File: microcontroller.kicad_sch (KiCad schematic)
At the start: 85 parts, among them CN10 JST BM06B-SRSS-TB(LF)(SN), CN11 BM05B-SRSS-TB(LF)(SN), CN2 Samtec FTSH-107-01-L-DV-K, CN3 104031-0811, CN4 M20-9990346, CN5 Molex 105057-0001, CN6 BM03B-SRSS-TB(LF)(SN), CN7 BM04B-SRSS-TB(LF)(SN), CN8 BM04B-SRSS-TB(LF)(SN), CN9 JST BM06B-SRSS-TB(LF)(SN), U2 STM32H743VIT6, U3 TMP102AIDRL, U4 Microchip 24AA256UIDT-I/ST

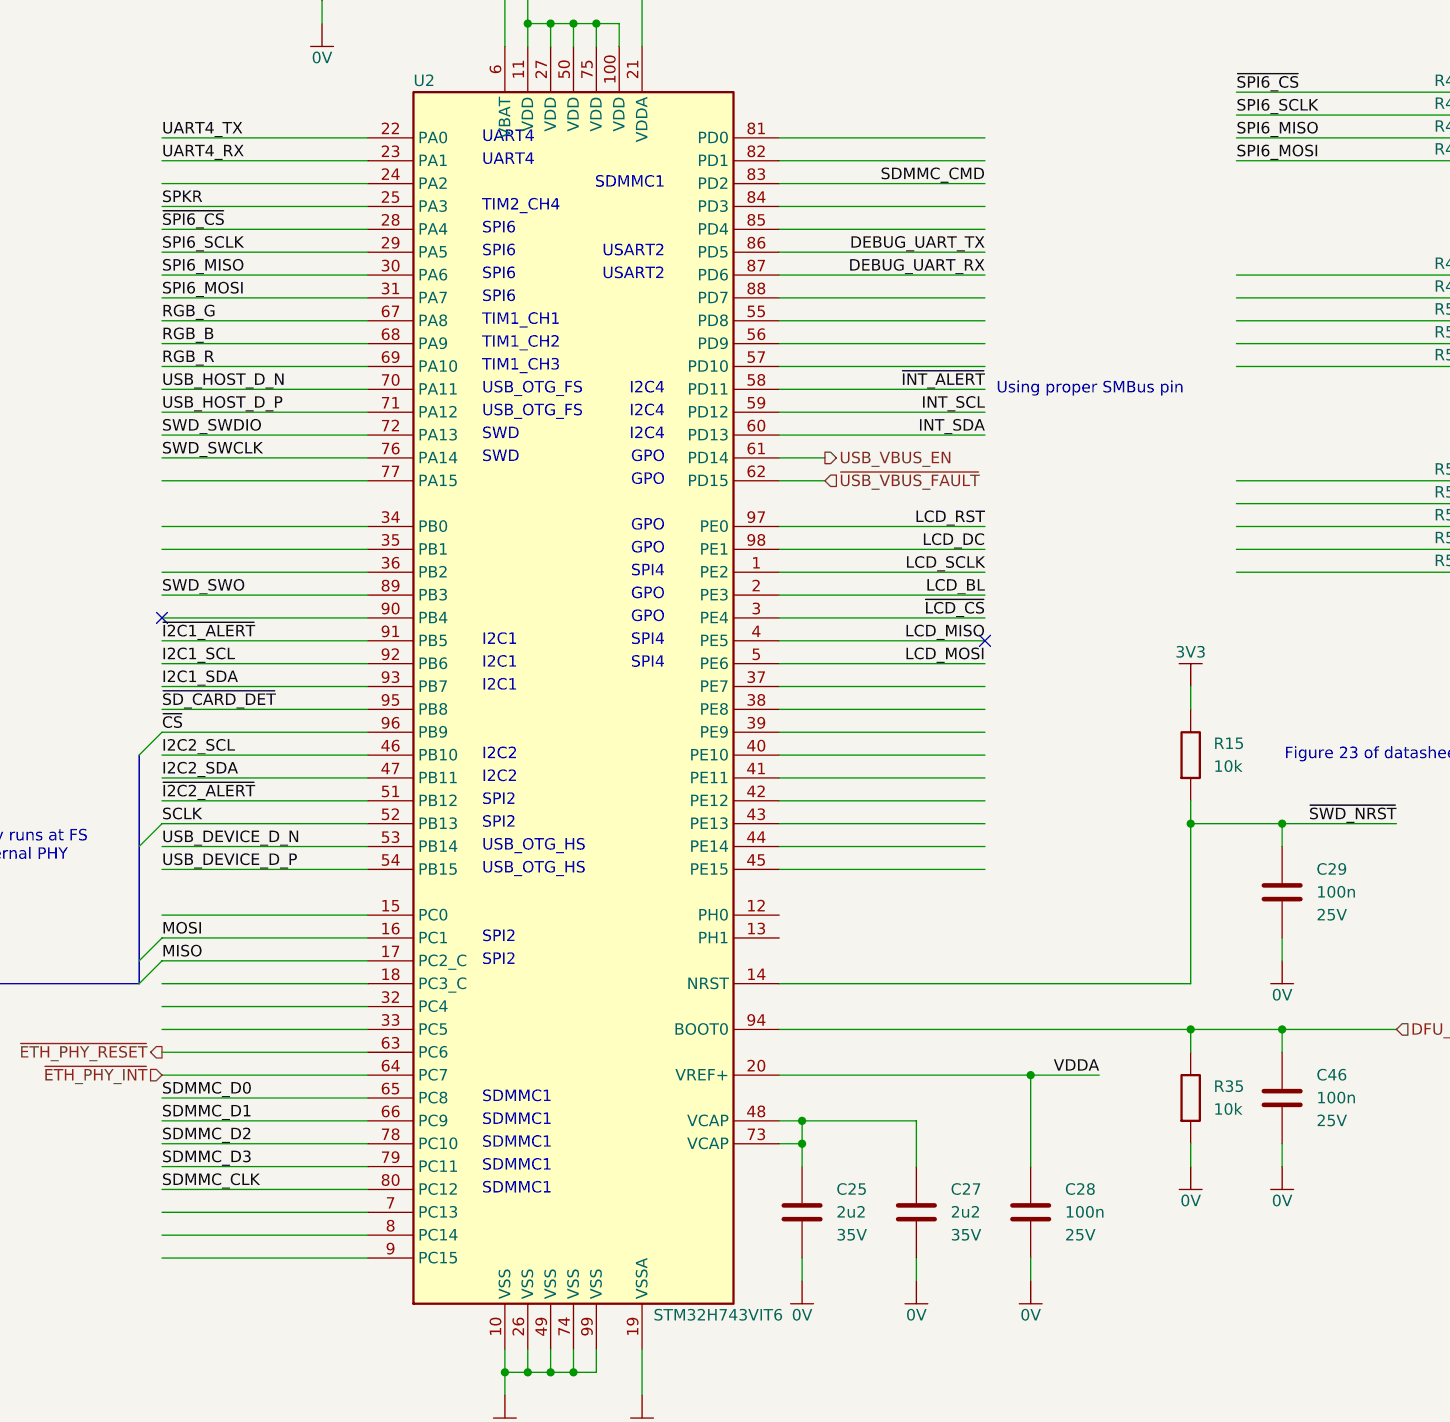
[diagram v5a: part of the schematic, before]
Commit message: headers now connected
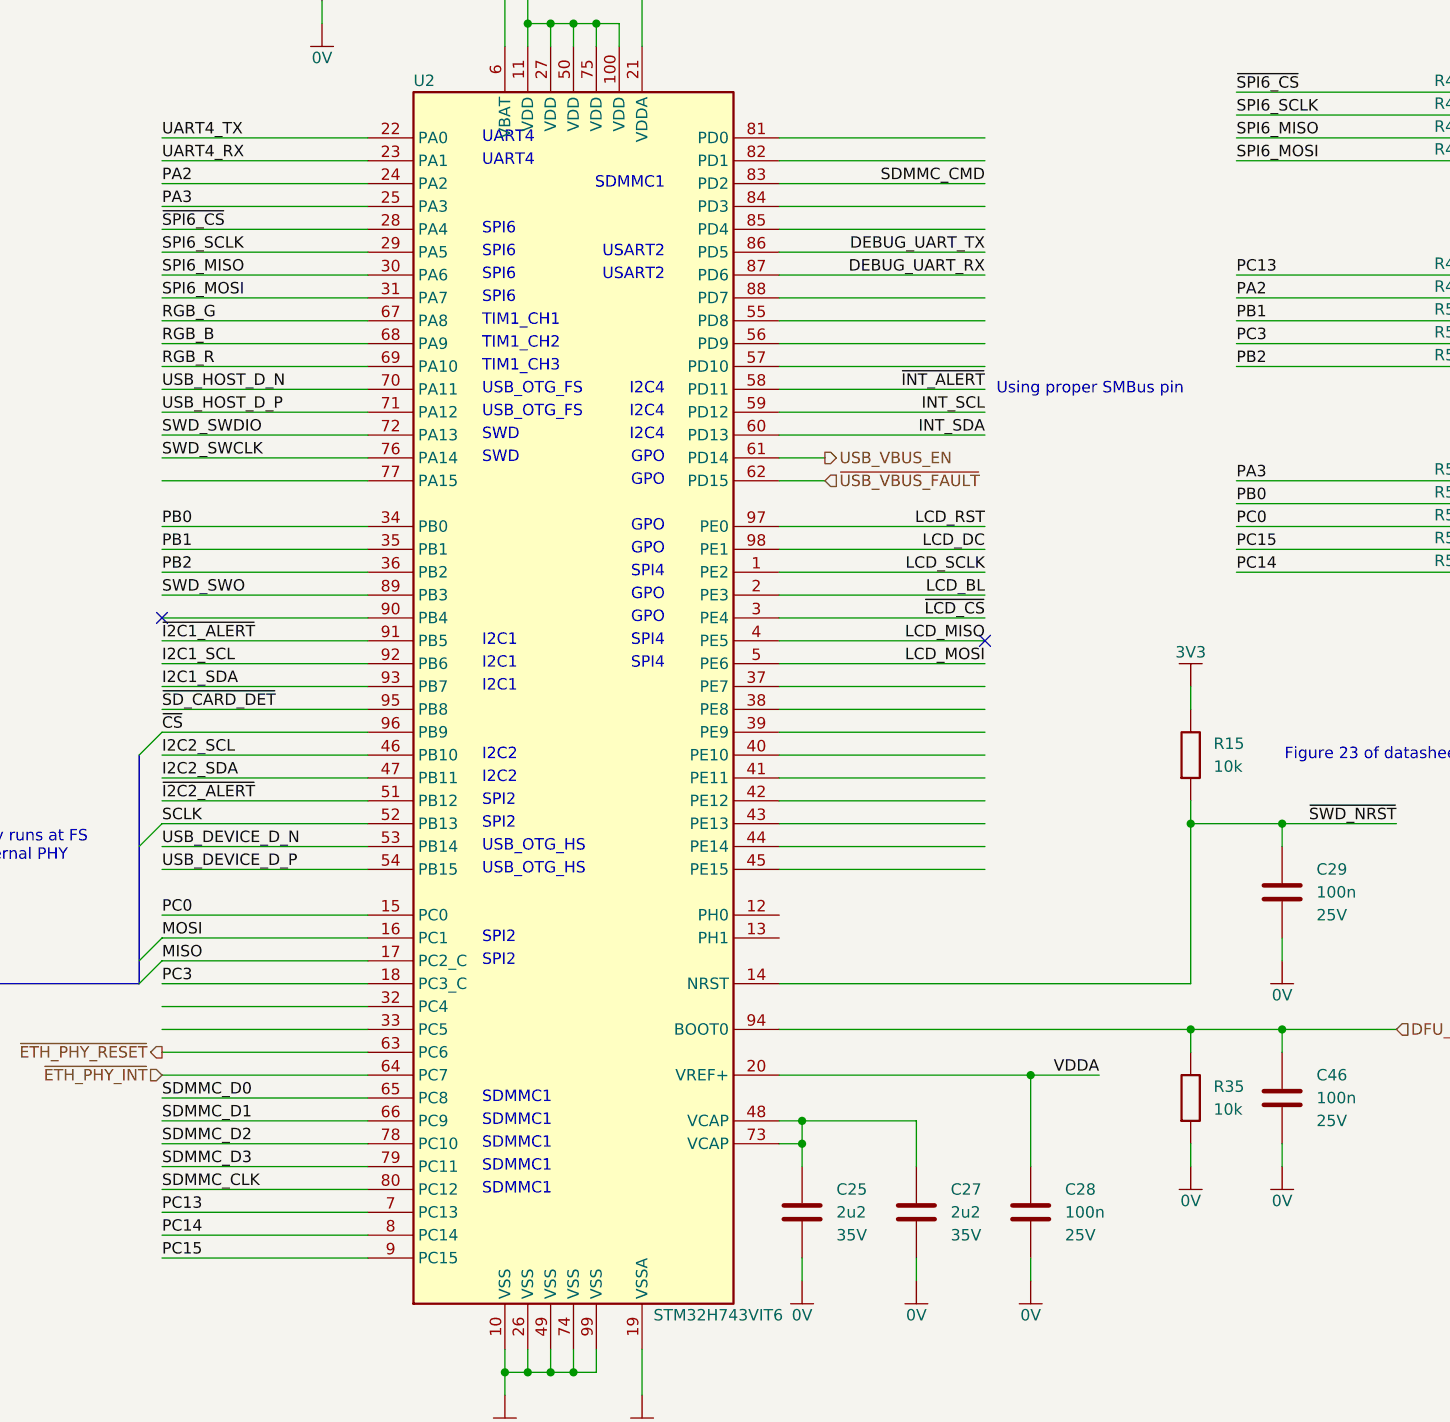
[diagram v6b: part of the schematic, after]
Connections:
- net SPKR is gone; now on net PA3: U2.25 (PA3)
- net PC15: now reaches R56.1
- net PC15: now also U2.9 (PC15)
- net PC14: now reaches R57.1
- net PC14: now also U2.8 (PC14)
- net PC0: now reaches R55.1
- net PC0: now also U2.15 (PC0)
- net PA3: now reaches R53.1
- net PC13: now reaches R48.1
- net PC13: now also U2.7 (PC13)
- net PC3: now reaches R51.1
- net PC3: now also U2.18 (PC3_C)
- net PB0: now reaches R54.1
- net PB0: now also U2.34 (PB0)
- net PB1: now reaches R50.1
- net PB1: now also U2.35 (PB1)
- net PB2: now reaches R52.1
- net PB2: now also U2.36 (PB2)
- net PA2: now reaches U2.24 (PA2)
- net PA2: now also R49.1
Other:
- note removed: "TIM2_CH4"
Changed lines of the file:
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@@
 		)
 	)
-	(text "TIM2_CH4"
-		(exclude_from_sim no)
-		(at 241.3 109.22 0)
-		(effects
-			(font
-				(size 1.27 1.27)
-			)
-			(justify left)
-		)
-	)
 	(text "I2C4"
 		(exclude_from_sim no)
@@
 	)
 	(no_connect
-		(at 297.18 157.48)
+		(at 48.26 63.5)
 	)
 	(no_connect
-		(at 48.26 63.5)
+		(at 297.18 157.48)
 	)
 	(no_connect
@@
 		)
 	)
+	(label "PA2"
+		(at 205.74 106.68 0)
+		(effects
+			(font
+				(size 1.27 1.27)
+			)
+			(justify left bottom)
+		)
+	)
+	(label "PC15"
+		(at 205.74 226.06 0)
+		(effects
+			(font
+				(size 1.27 1.27)
+			)
+			(justify left bottom)
+		)
+	)
 	(label "INT_SDA"
 		(at 160.02 256.54 180)
@@
 		)
 	)
-	(label "SPKR"
-		(at 205.74 109.22 0)
+	(label "~{LCD_CS}"
+		(at 297.18 154.94 180)
 		(effects
 			(font
 				(size 1.27 1.27)
 			)
-			(justify left bottom)
+			(justify right bottom)
 		)
 	)
-	(label "~{LCD_CS}"
-		(at 297.18 154.94 180)
+	(label "PC14"
+		(at 325.12 149.86 0)
 		(effects
 			(font
 				(size 1.27 1.27)
 			)
-			(justify right bottom)
+			(justify left bottom)
 		)
 	)
@@
 		)
 	)
+	(label "PA3"
+		(at 325.12 139.7 0)
+		(effects
+			(font
+				(size 1.27 1.27)
+			)
+			(justify left bottom)
+		)
+	)
 	(label "I2C1_SDA"
 		(at 205.74 162.56 0)
@@
 		)
 	)
+	(label "PB0"
+		(at 205.74 144.78 0)
+		(effects
+			(font
+				(size 1.27 1.27)
+			)
+			(justify left bottom)
+		)
+	)
 	(label "SCLK"
 		(at 205.74 177.8 0)
@@
 		)
 	)
+	(label "PC0"
+		(at 325.12 144.78 0)
+		(effects
+			(font
+				(size 1.27 1.27)
+			)
+			(justify left bottom)
+		)
+	)
+	(label "LCD_MISO"
+		(at 297.18 157.48 180)
+		(effects
+			(font
+				(size 1.27 1.27)
+			)
+			(justify right bottom)
+		)
+	)
 	(label "~{INT_ALERT}"
 		(at 81.28 259.08 180)
@@
 		)
 	)
+	(label "PC0"
+		(at 205.74 187.96 0)
+		(effects
+			(font
+				(size 1.27 1.27)
+			)
+			(justify left bottom)
+		)
+	)
 	(label "INT_SDA"
 		(at 297.18 134.62 180)
@@
 		)
 	)
+	(label "PB0"
+		(at 325.12 142.24 0)
+		(effects
+			(font
+				(size 1.27 1.27)
+			)
+			(justify left bottom)
+		)
+	)
 	(label "~{I2C2_ALERT}"
 		(at 205.74 175.26 0)
@@
 		)
 	)
+	(label "PB1"
+		(at 205.74 147.32 0)
+		(effects
+			(font
+				(size 1.27 1.27)
+			)
+			(justify left bottom)
+		)
+	)
 	(label "MOSI"
 		(at 205.74 190.5 0)
@@
 		)
 	)
+	(label "PB2"
+		(at 325.12 127 0)
+		(effects
+			(font
+				(size 1.27 1.27)
+			)
+			(justify left bottom)
+		)
+	)
 	(label "DEBUG_UART_RX"
 		(at 297.18 116.84 180)
@@
 		)
 	)
+	(label "PC15"
+		(at 325.12 147.32 0)
+		(effects
+			(font
+				(size 1.27 1.27)
+			)
+			(justify left bottom)
+		)
+	)
 	(label "I2C2_SDA"
 		(at 205.74 172.72 0)
@@
 		)
 	)
+	(label "PA2"
+		(at 325.12 119.38 0)
+		(effects
+			(font
+				(size 1.27 1.27)
+			)
+			(justify left bottom)
+		)
+	)
+	(label "PC3"
+		(at 325.12 124.46 0)
+		(effects
+			(font
+				(size 1.27 1.27)
+			)
+			(justify left bottom)
+		)
+	)
 	(label "LCD_SCLK"
 		(at 297.18 149.86 180)
@@
 		)
 	)
+	(label "PC13"
+		(at 205.74 220.98 0)
+		(effects
+			(font
+				(size 1.27 1.27)
+			)
+			(justify left bottom)
+		)
+	)
 	(label "RGB_G"
 		(at 205.74 121.92 0)
@@
 		)
 	)
-	(label "LCD_MISO"
-		(at 297.18 157.48 180)
+	(label "LCD_MOSI"
+		(at 111.76 210.82 0)
 		(effects
 			(font
 				(size 1.27 1.27)
 			)
-			(justify right bottom)
+			(justify left bottom)
 		)
 	)
-	(label "LCD_MOSI"
-		(at 111.76 210.82 0)
+	(label "UART4_RX"
+		(at 325.12 48.26 0)
 		(effects
 			(font
@@
 		)
 	)
-	(label "UART4_RX"
-		(at 325.12 48.26 0)
+	(label "PC13"
+		(at 325.12 116.84 0)
 		(effects
 			(font
@@
 		)
 	)
+	(label "PA3"
+		(at 205.74 109.22 0)
+		(effects
+			(font
+				(size 1.27 1.27)
+			)
+			(justify left bottom)
+		)
+	)
 	(label "SWD_SWDIO"
 		(at 132.08 55.88 180)
@@
 		)
 	)
+	(label "PC3"
+		(at 205.74 195.58 0)
+		(effects
+			(font
+				(size 1.27 1.27)
+			)
+			(justify left bottom)
+		)
+	)
 	(label "MISO"
 		(at 205.74 193.04 0)
@@
 		)
 	)
+	(label "PB1"
+		(at 325.12 121.92 0)
+		(effects
+			(font
+				(size 1.27 1.27)
+			)
+			(justify left bottom)
+		)
+	)
 	(label "~{CS}"
 		(at 205.74 167.64 0)
@@
 		)
 	)
+	(label "PB2"
+		(at 205.74 149.86 0)
+		(effects
+			(font
+				(size 1.27 1.27)
+			)
+			(justify left bottom)
+		)
+	)
+	(label "PC14"
+		(at 205.74 223.52 0)
+		(effects
+			(font
+				(size 1.27 1.27)
+			)
+			(justify left bottom)
+		)
+	)
